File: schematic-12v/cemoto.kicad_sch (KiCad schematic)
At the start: 46 parts, among them J1 laturi, J2 Conn_USB, J3 Conn_GPS, SW1 virtalukko, SW2 torvi, SW3 lahikauko, SW4 brake, SW5 turn, SW6 hazard, U1 TAICO BE48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

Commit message: schematic-12v update
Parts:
- removed BT1, BT2, BT3, BT4, BT6, BT7, BT8: bat, symbol Device:Battery_Cell
- removed U1: TAICO BE48, symbol cemoto:battery_equalizer_be48
- added J?: USB_charger_DCDC5v_waterproof, symbol Connector_Generic:Conn_01x02
- added J?: laturi30A, symbol Connector_Generic:Conn_01x02
- added SW?: clear_trip, symbol Switch:SW_Push
- added U?: odometer, symbol cemoto:odometer
- added U?: speed_limiter, symbol cemoto:speed_limiter
- J1: value laturi -> laturi7A
- J3: value Conn_GPS -> Conn_USB_2
- renumbered BT5 to BT1
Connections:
- net +12V: now also F6.1, U?.6 (LED_12V)
- net +5V: now also J2.1 (Pin_1); no longer F6.1
- net GND: now also J?.1 (Pin_1), J?.2 (Pin_2), U?.3 (GND), U?.7 (LED_GND)
- net VBAT: now also J?.2 (Pin_2)
- net at U2.15 (THROTTLE_5V): now also U?.1 (+5V); no longer RV1.1
- net at U2.16 (THROTTLE_IN): now also U?.5 (HAND_BLDC); no longer RV1.2
- net at U2.5 (THROTTLE_GND): now also U?.2 (GND); no longer RV1.3
- net at U2.6 (+5V): now also U?.1 (+5V)
- net at U2.7 (HALL_A): now also U?.4 (HALL), U?.5 (HALL)
- net at R1.1: now also BT1.2 (-); no longer MES2.1 (-)
- net at MES1.1 (-), R1.3: now also MES2.1 (-)
- net +48V: now reaches BT1.1 (+), F1.2
- net at F6.2: now also J?.1 (Pin_1); no longer J2.1 (Pin_1)
- new net: SW?.1, U?.2 (BTN)
- new net: SW?.2, U?.4 (GND)
- new net: RV1.1, U?.3 (GND), U?.6 (HAND_IN)
- new net: RV1.3, U?.7 (HAND_OUT)
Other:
- note added: "16s LiFePo4 cells -> 16*3.65 = 58.4v Daly BMS 150A Qucc 10A active balancer"
- note added: "kojelaudan virtamittari"
- moved on the sheet: BT1, F1, F6, J1, M?, MES1, MES2, R1, RV1, SW1, U2

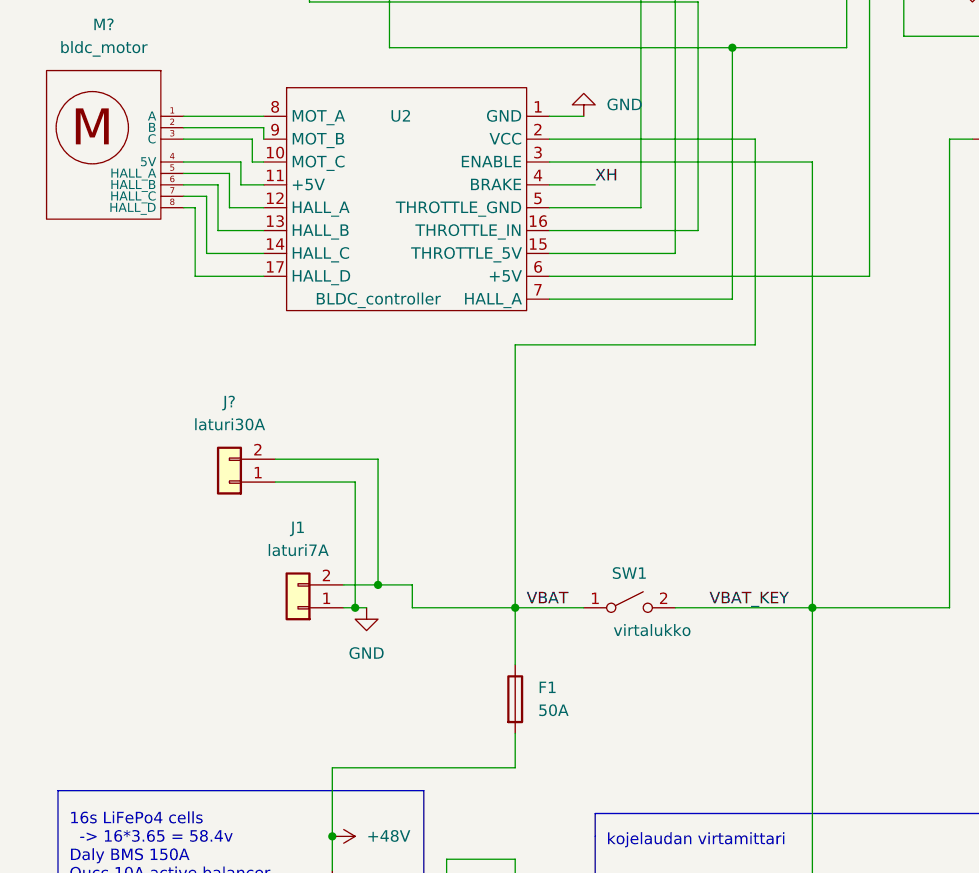
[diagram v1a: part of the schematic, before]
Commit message: update kicad version, add charger relay
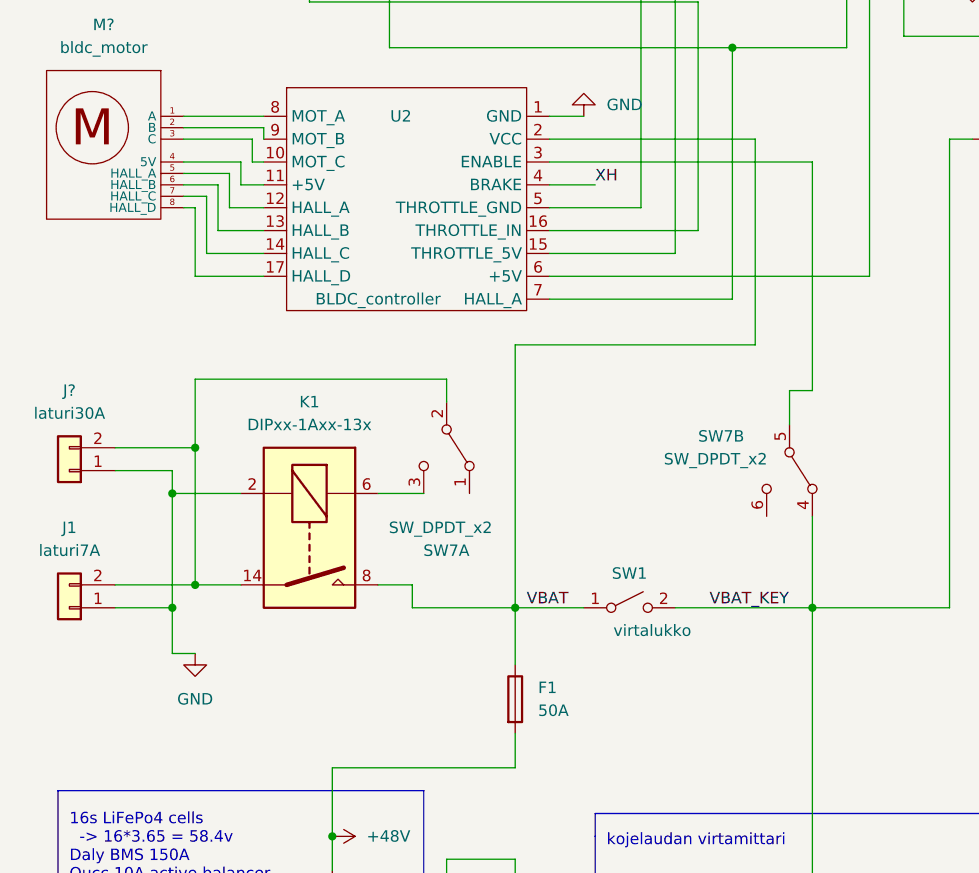
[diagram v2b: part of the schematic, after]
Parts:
- added K1: DIPxx-1Axx-13x, Relay_THT:Relay_StandexMeder_DIP_LowProfile, symbol Relay:DIPxx-1Axx-13x
- added SW7: SW_DPDT_x2, symbol Switch:SW_DPDT_x2
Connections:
- net GND: now also K1.2
- net VBAT: now also K1.8; no longer J1.2 (Pin_2), J?.2 (Pin_2)
- net VBAT_KEY: now also SW7.4 (A); no longer U2.3 (ENABLE)
- new net: SW7.5 (B), U2.3 (ENABLE)
- new net: J1.2 (Pin_2), J?.2 (Pin_2), K1.14, SW7.2 (B)
- new net: K1.6, SW7.3 (C)
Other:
- moved on the sheet: J1, J?
